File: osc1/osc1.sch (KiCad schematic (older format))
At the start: 58 parts, among them J1 LinFM, J10 PWMControl, J2 Hard Sync +, J3 Hard Sync -, J4 VOct, J5 Soft Sync Input, J6 Conn_02x08_Odd_Even, J7 Triangular Wave Output, J8 Square Wave Output, J9 Saw Wave Output, U1 AS3340, U2 TL072, U3 TL072

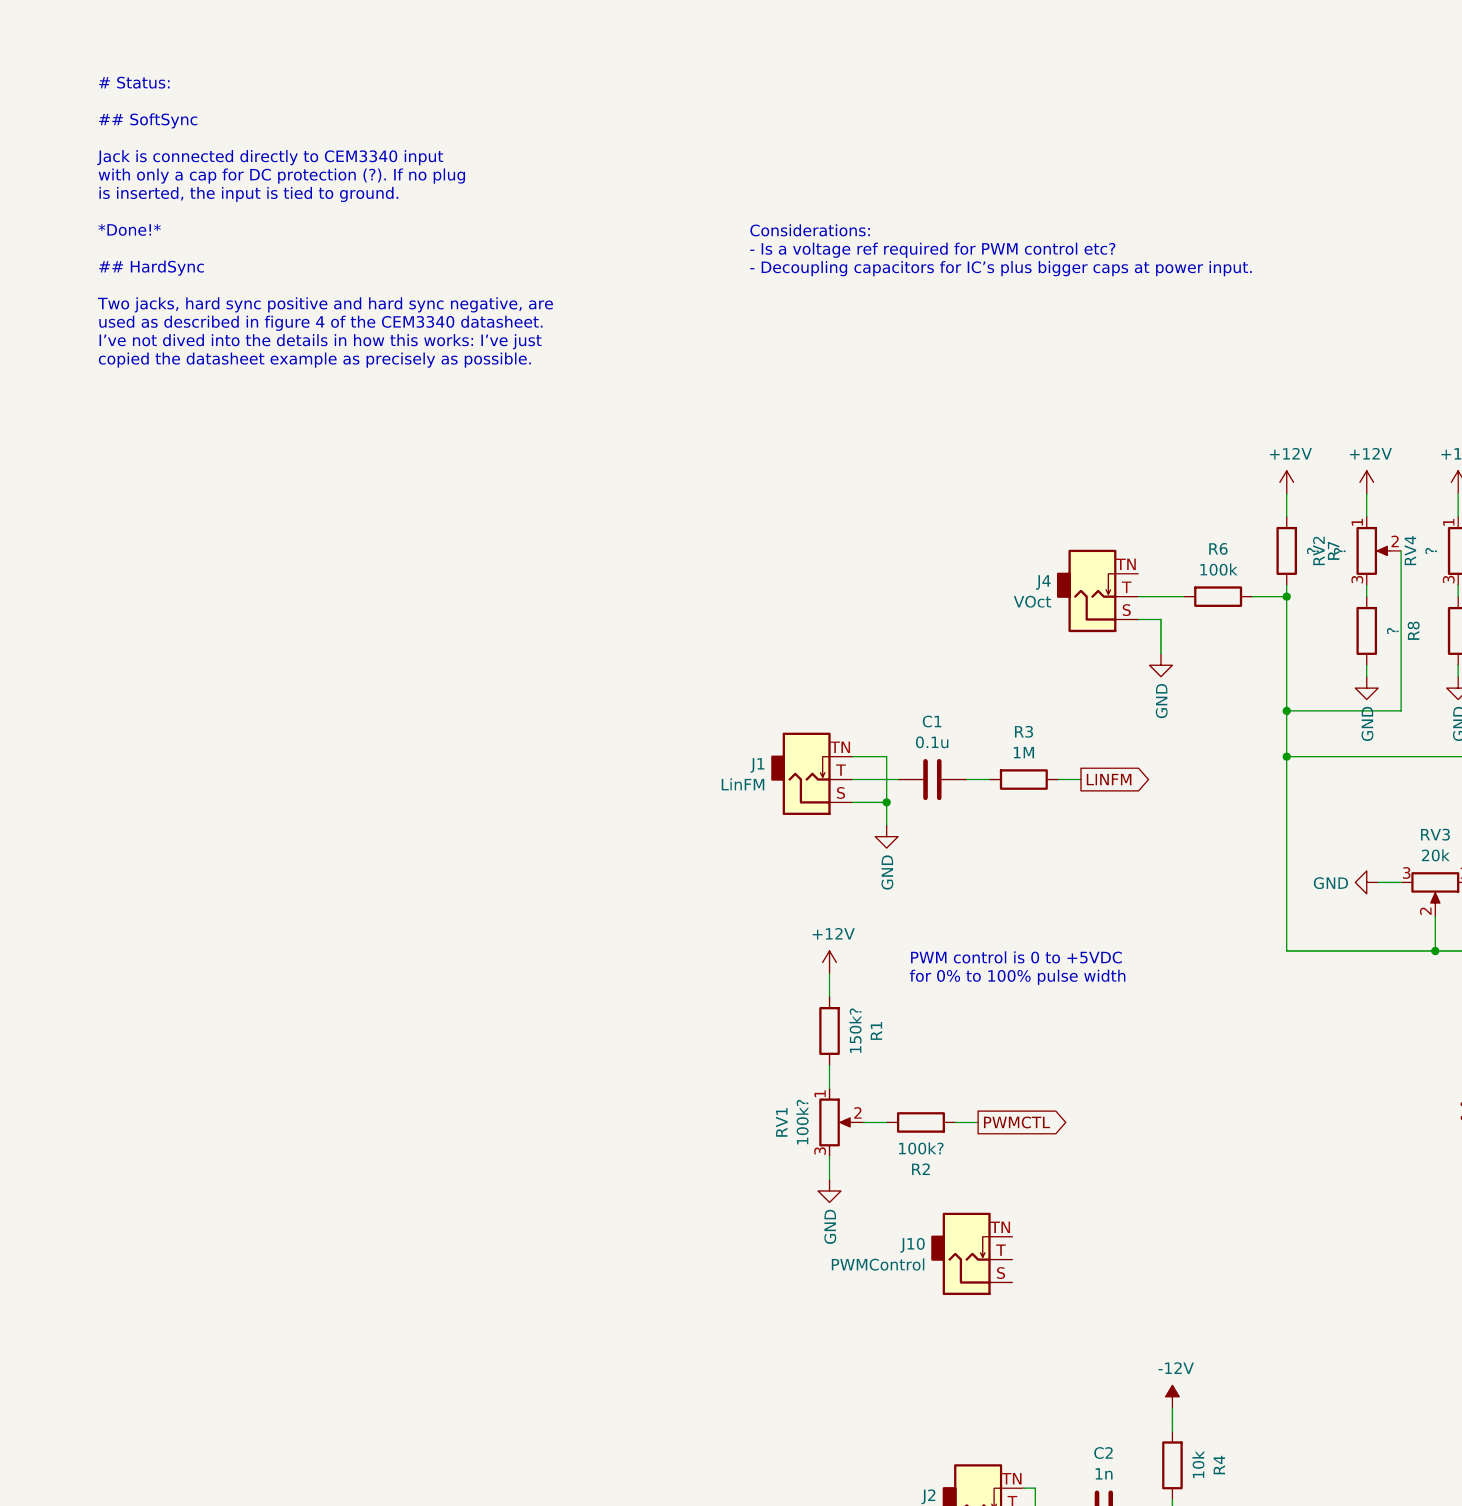
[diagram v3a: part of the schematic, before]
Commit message: PWM input (same config as d376f1211e99)
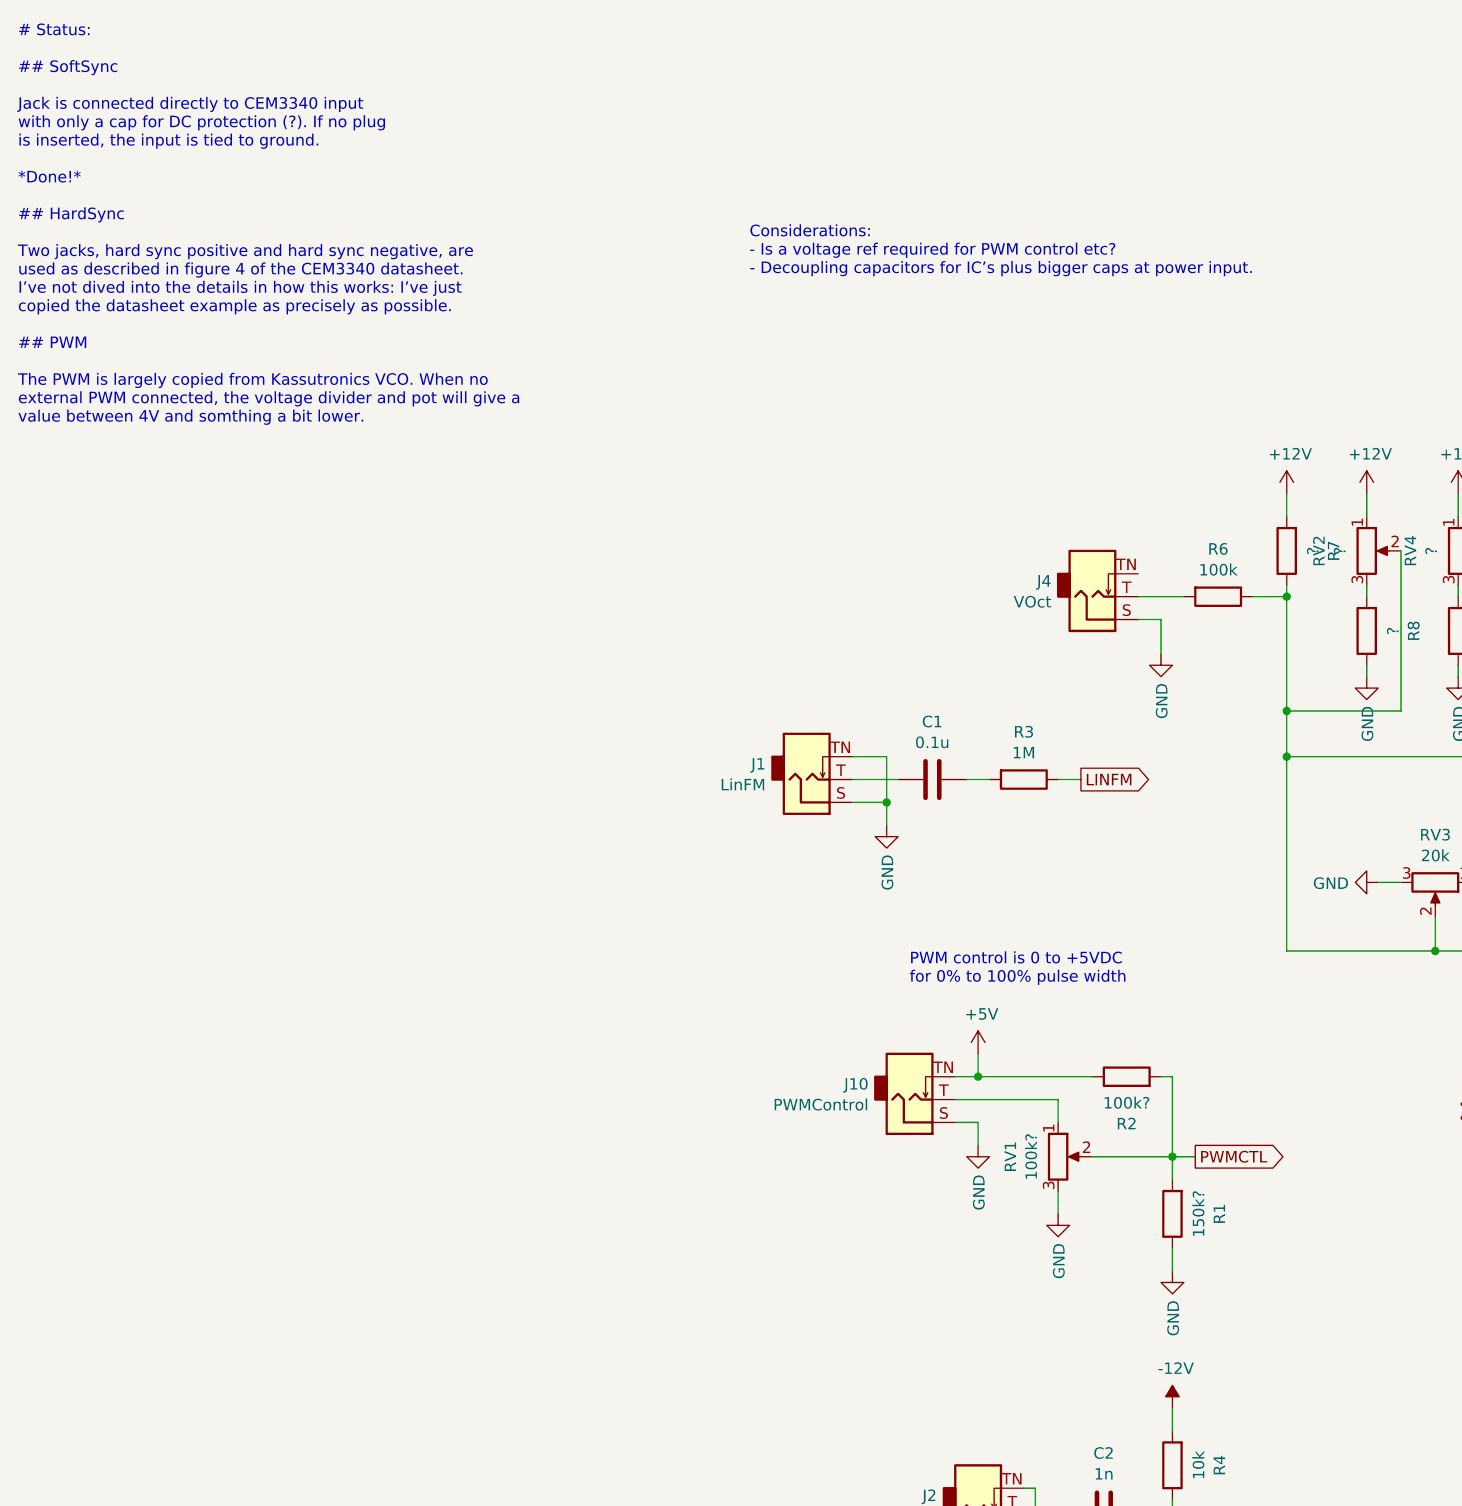
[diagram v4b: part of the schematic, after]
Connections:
- net +12V: no longer R1.2
- net +5V: now also J10.TN, R2.1
- net GND: now also J10.S, R1.1
- net PWMCTL: now also R1.2, RV1.2
- net at RV1.1: now also J10.T; no longer R1.1
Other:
- moved on the sheet: J10, R1, R2, RV1
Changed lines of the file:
@@
 L Device:R_POT RV1
 U 1 1 5DCC115F
-P 850 4450
-F 0 "RV1" V 643 4450 50  0000 C CNN
-F 1 "100k?" V 734 4450 50  0000 C CNN
-F 2 "Potentiometer_THT:Potentiometer_Alpha_RD901F-40-00D_Single_Vertical_CircularHoles" H 850 4450 50  0001 C CNN
-F 3 "~" H 850 4450 50  0001 C CNN
-	1    850  4450
-	1    0    0    -1
-$EndComp
-$Comp
-L power:+12V #PWR0123
-U 1 1 5DCCB73D
-P 850 3800
-F 0 "#PWR0123" H 850 3650 50  0001 C CNN
-F 1 "+12V" H 865 3973 50  0000 C CNN
-F 2 "" H 850 3800 50  0001 C CNN
-F 3 "" H 850 3800 50  0001 C CNN
-	1    850  3800
+P 1850 4600
+F 0 "RV1" V 1643 4600 50  0000 C CNN
+F 1 "100k?" V 1734 4600 50  0000 C CNN
+F 2 "Potentiometer_THT:Potentiometer_Alpha_RD901F-40-00D_Single_Vertical_CircularHoles" H 1850 4600 50  0001 C CNN
+F 3 "~" H 1850 4600 50  0001 C CNN
+	1    1850 4600
 	1    0    0    -1
 $EndComp
@@
 L Device:R R1
 U 1 1 5DCCC2FE
-P 850 4050
-F 0 "R1" V 643 4050 50  0000 C CNN
-F 1 "150k?" V 734 4050 50  0000 C CNN
-F 2 "Resistor_SMD:R_0603_1608Metric" V 780 4050 50  0001 C CNN
-F 3 "~" H 850 4050 50  0001 C CNN
-	1    850  4050
+P 2350 4850
+F 0 "R1" V 2143 4850 50  0000 C CNN
+F 1 "150k?" V 2234 4850 50  0000 C CNN
+F 2 "Resistor_SMD:R_0603_1608Metric" V 2280 4850 50  0001 C CNN
+F 3 "~" H 2350 4850 50  0001 C CNN
+	1    2350 4850
 	-1   0    0    1
 $EndComp
-Wire Wire Line
-	850  3900 850  3800
-Wire Wire Line
-	850  4200 850  4300
 $Comp
 L power:GND #PWR0124
 U 1 1 5DCD529A
-P 850 4700
-F 0 "#PWR0124" H 850 4450 50  0001 C CNN
-F 1 "GND" V 855 4572 50  0000 R CNN
-F 2 "" H 850 4700 50  0001 C CNN
-F 3 "" H 850 4700 50  0001 C CNN
-	1    850  4700
-	1    0    0    -1
-$EndComp
-Wire Wire Line
-	850  4700 850  4600
+P 1850 4850
+F 0 "#PWR0124" H 1850 4600 50  0001 C CNN
+F 1 "GND" V 1855 4722 50  0000 R CNN
+F 2 "" H 1850 4850 50  0001 C CNN
+F 3 "" H 1850 4850 50  0001 C CNN
+	1    1850 4850
+	1    0    0    -1
+$EndComp
+Wire Wire Line
+	1850 4850 1850 4750
 $Comp
 L Device:R R2
 U 1 1 5DCD9BD4
-P 1250 4450
-F 0 "R2" V 1043 4450 50  0000 C CNN
-F 1 "100k?" V 1134 4450 50  0000 C CNN
-F 2 "Resistor_SMD:R_0603_1608Metric" V 1180 4450 50  0001 C CNN
-F 3 "~" H 1250 4450 50  0001 C CNN
-	1    1250 4450
+P 2150 4250
+F 0 "R2" V 1943 4250 50  0000 C CNN
+F 1 "100k?" V 2034 4250 50  0000 C CNN
+F 2 "Resistor_SMD:R_0603_1608Metric" V 2080 4250 50  0001 C CNN
+F 3 "~" H 2150 4250 50  0001 C CNN
+	1    2150 4250
 	0    -1   -1   0
 $EndComp
-Wire Wire Line
-	1000 4450 1100 4450
-Wire Wire Line
-	1400 4450 1500 4450
-Text GLabel 1500 4450 2    50   Output ~ 0
+Text GLabel 2450 4600 2    50   Output ~ 0
 PWMCTL
 Text Notes 1200 3850 0    50   ~ 0
@@
 	4900 6950 4900 7150
 Connection ~ 4900 7150
-Text Notes -2350 1150 0    50   ~ 0
-# Status:\n\n## SoftSync\n\nJack is connected directly to CEM3340 input\nwith only a cap for DC protection (?). If no plug\nis inserted, the input is tied to ground.\n\n*Done!*\n\n## HardSync\n\nTwo jacks, hard sync positive and hard sync negative, are\nused as described in figure 4 of the CEM3340 datasheet.\nI’ve not dived into the details in how this works: I’ve just\ncopied the datasheet example as precisely as possible.
+Text Notes -2700 1400 0    50   ~ 0
+# Status:\n\n## SoftSync\n\nJack is connected directly to CEM3340 input\nwith only a cap for DC protection (?). If no plug\nis inserted, the input is tied to ground.\n\n*Done!*\n\n## HardSync\n\nTwo jacks, hard sync positive and hard sync negative, are\nused as described in figure 4 of the CEM3340 datasheet.\nI’ve not dived into the details in how this works: I’ve just\ncopied the datasheet example as precisely as possible.\n\n## PWM\n\nThe PWM is largely copied from Kassutronics VCO. When no\nexternal PWM connected, the voltage divider and pot will give a\nvalue between 4V and somthing a bit lower.
 Wire Wire Line
 	1700 6050 1750 6050
@@
 L Connector:AudioJack2_SwitchT J10
 U 1 1 5E71DBC6
-P 1450 5050
-F 0 "J10" H 1271 4983 50  0000 R CNN
-F 1 "PWMControl" H 1271 5074 50  0000 R CNN
-F 2 "Connector_Audio:Jack_3.5mm_QingPu_WQP-PJ398SM_Vertical_CircularHoles" H 1450 5050 50  0001 C CNN
-F 3 "~" H 1450 5050 50  0001 C CNN
-	1    1450 5050
+P 1200 4350
+F 0 "J10" H 1021 4283 50  0000 R CNN
+F 1 "PWMControl" H 1021 4374 50  0000 R CNN
+F 2 "Connector_Audio:Jack_3.5mm_QingPu_WQP-PJ398SM_Vertical_CircularHoles" H 1200 4350 50  0001 C CNN
+F 3 "~" H 1200 4350 50  0001 C CNN
+	1    1200 4350
 	1    0    0    1
 $EndComp
+$Comp
+L power:+5V #PWR?
+U 1 1 5E8B4A79
+P 1500 4150
+F 0 "#PWR?" H 1500 4000 50  0001 C CNN
+F 1 "+5V" H 1515 4323 50  0000 C CNN
+F 2 "" H 1500 4150 50  0001 C CNN
+F 3 "" H 1500 4150 50  0001 C CNN
+	1    1500 4150
+	1    0    0    -1
+$EndComp
+Wire Wire Line
+	1400 4250 1500 4250
+Wire Wire Line
+	1500 4250 1500 4150
+$Comp
+L power:GND #PWR?
+U 1 1 5E8BF9F3
+P 1500 4550
+F 0 "#PWR?" H 1500 4300 50  0001 C CNN
+F 1 "GND" V 1505 4422 50  0000 R CNN
+F 2 "" H 1500 4550 50  0001 C CNN
+F 3 "" H 1500 4550 50  0001 C CNN
+	1    1500 4550
+	1    0    0    -1
+$EndComp
+Wire Wire Line
+	1400 4450 1500 4450
+Wire Wire Line
+	1500 4450 1500 4550
+Wire Wire Line
+	1500 4250 2000 4250
+Connection ~ 1500 4250
+Wire Wire Line
+	1400 4350 1850 4350
+Wire Wire Line
+	1850 4350 1850 4450
+Wire Wire Line
+	2350 4600 2350 4250
+Wire Wire Line
+	2350 4250 2300 4250
+Wire Wire Line
+	2000 4600 2350 4600
+$Comp
+L power:GND #PWR?
+U 1 1 5E9C47B8
+P 2350 5100
+F 0 "#PWR?" H 2350 4850 50  0001 C CNN
+F 1 "GND" V 2355 4972 50  0000 R CNN
+F 2 "" H 2350 5100 50  0001 C CNN
+F 3 "" H 2350 5100 50  0001 C CNN
+	1    2350 5100
+	1    0    0    -1
+$EndComp
+Wire Wire Line
+	2350 5100 2350 5000
+Wire Wire Line
+	2350 4700 2350 4600
+Connection ~ 2350 4600
+Wire Wire Line
+	2350 4600 2450 4600
 $EndSCHEMATC

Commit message: osc1: plan component placement
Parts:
- D1, D2: footprint Diode_THT:D_DO-35_SOD27_P7.62mm_Horizontal -> Diode_SMD:D_SOD-523
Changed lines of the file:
@@
 F 0 "D1" V 2396 6271 50  0000 R CNN
 F 1 "1N914" V 2305 6271 50  0000 R CNN
-F 2 "Diode_THT:D_DO-35_SOD27_P7.62mm_Horizontal" H 2350 6175 50  0001 C CNN
+F 2 "Diode_SMD:D_SOD-523" H 2350 6175 50  0001 C CNN
 F 3 "http://www.vishay.com/docs/85622/1n914.pdf" H 2350 6350 50  0001 C CNN
 	1    2350 6350
@@
 F 0 "D2" V 2396 6771 50  0000 R CNN
 F 1 "1N914" V 2305 6771 50  0000 R CNN
-F 2 "Diode_THT:D_DO-35_SOD27_P7.62mm_Horizontal" H 2350 6675 50  0001 C CNN
+F 2 "Diode_SMD:D_SOD-523" H 2350 6675 50  0001 C CNN
 F 3 "http://www.vishay.com/docs/85622/1n914.pdf" H 2350 6850 50  0001 C CNN
 	1    2350 6850
@@
 $EndComp
 $Comp
-L power:+5V #PWR?
+L power:+5V #PWR0123
 U 1 1 5E8B4A79
 P 1500 4150
-F 0 "#PWR?" H 1500 4000 50  0001 C CNN
+F 0 "#PWR0123" H 1500 4000 50  0001 C CNN
 F 1 "+5V" H 1515 4323 50  0000 C CNN
 F 2 "" H 1500 4150 50  0001 C CNN
@@
 	1500 4250 1500 4150
 $Comp
-L power:GND #PWR?
+L power:GND #PWR0140
 U 1 1 5E8BF9F3
 P 1500 4550
-F 0 "#PWR?" H 1500 4300 50  0001 C CNN
+F 0 "#PWR0140" H 1500 4300 50  0001 C CNN
 F 1 "GND" V 1505 4422 50  0000 R CNN
 F 2 "" H 1500 4550 50  0001 C CNN
@@
 	2000 4600 2350 4600
 $Comp
-L power:GND #PWR?
+L power:GND #PWR0141
 U 1 1 5E9C47B8
 P 2350 5100
-F 0 "#PWR?" H 2350 4850 50  0001 C CNN
+F 0 "#PWR0141" H 2350 4850 50  0001 C CNN
 F 1 "GND" V 2355 4972 50  0000 R CNN
 F 2 "" H 2350 5100 50  0001 C CNN

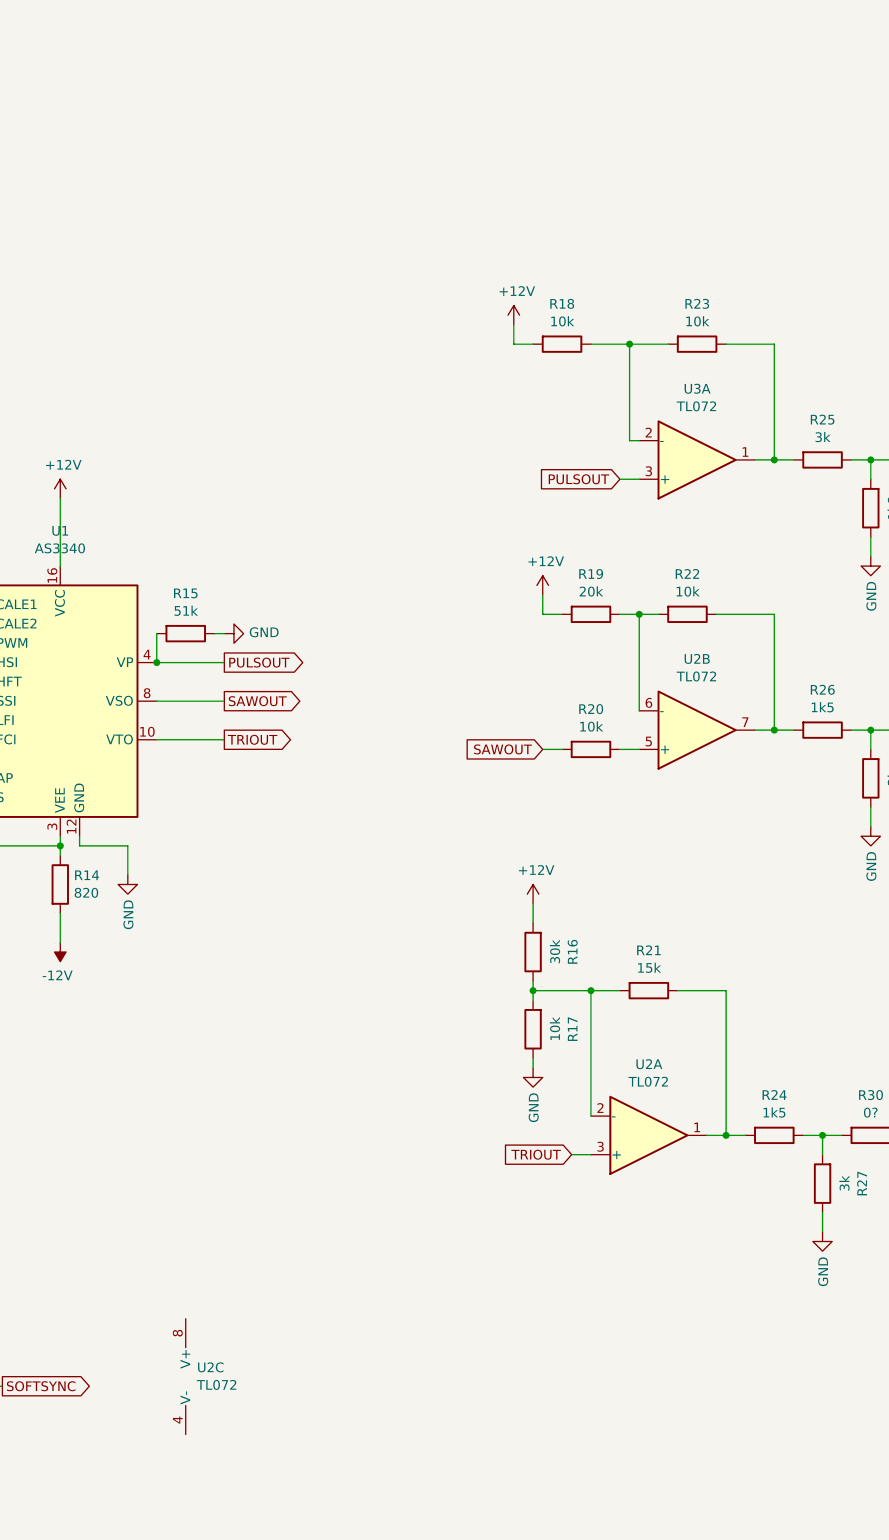
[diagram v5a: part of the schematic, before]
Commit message: osc1: all but 6 traces routed (crudely)
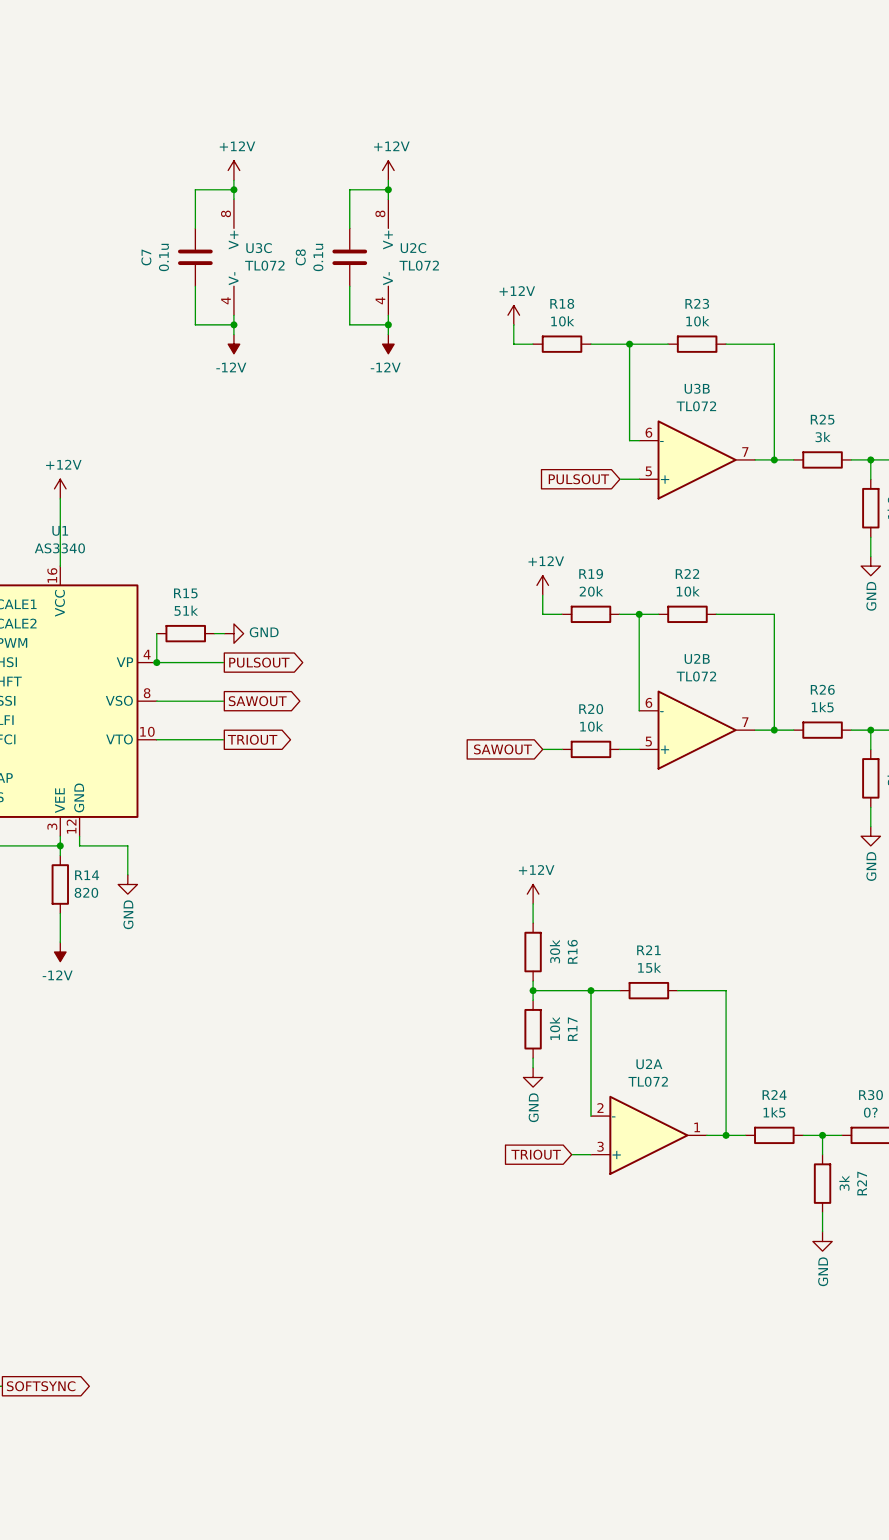
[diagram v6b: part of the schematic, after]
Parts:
- removed U3: TL072, Package_SO:SO-8_3.9x4.9mm_P1.27mm, symbol Amplifier_Operational:TL072
- added C7, C8: 0.1u, Capacitor_SMD:C_0603_1608Metric, symbol Device:C
- added U3: TL072, Package_SO:SO-8_3.9x4.9mm_P1.27mm, symbol Amplifier_Operational:TL072
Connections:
- net +12V: now also U2.8 (V+), C7.1, C8.1, U3.8 (V+)
- net -12V: now also U2.4 (V-), C7.2, C8.2, U3.4 (V-)
- net PULSOUT: now also U3.5 (+)
- net at R23.1, R25.2: now also U3.7
- net at R18.1, R23.2: now also U3.6 (-)
